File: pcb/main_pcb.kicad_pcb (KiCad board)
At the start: 2 copper layers, 62 x 67 mm, 43 parts, among them J1 Conn_01x06_Socket, J4 USB_C_Receptacle_USB2.0, Q1 Si2323DS, SW1 SW_Push, SW2 SW_Push, SW3 SW_Push, U1 ESP32-H2-MINI-1, U2 LM5165Y, Y1 32.768KHz

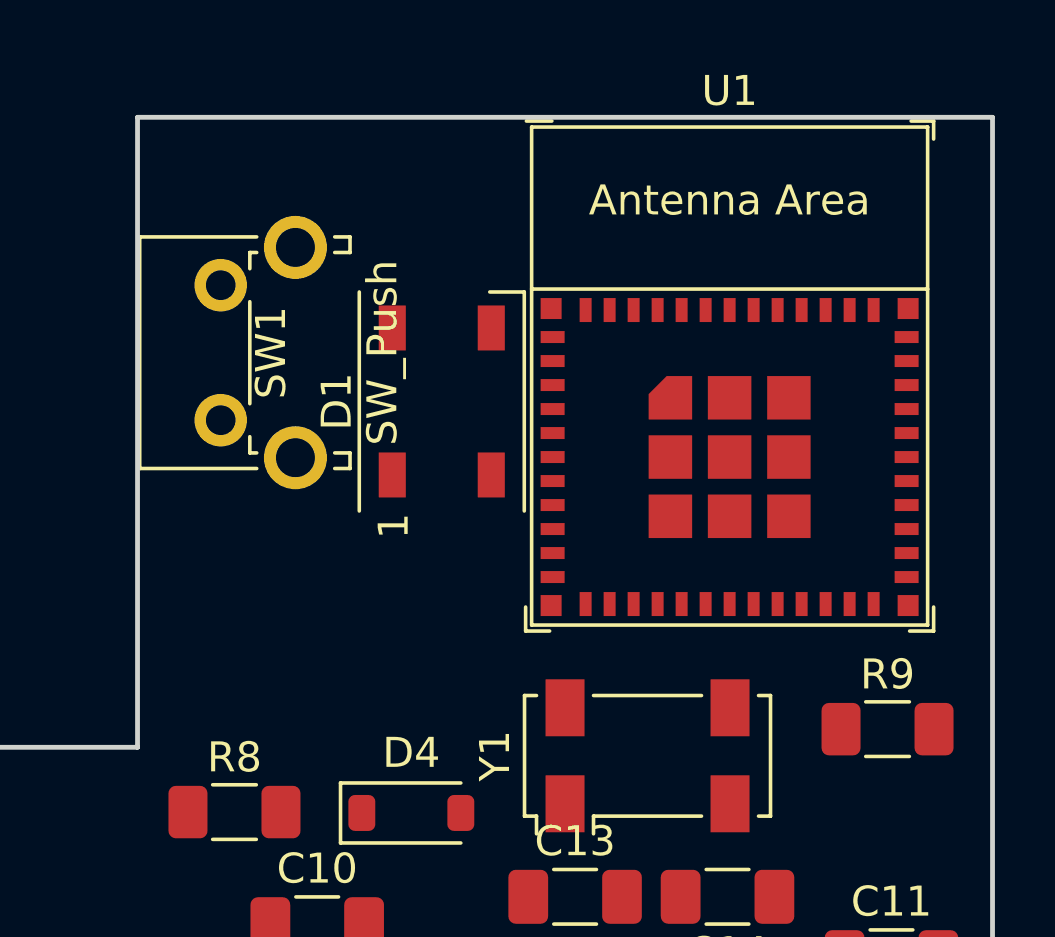
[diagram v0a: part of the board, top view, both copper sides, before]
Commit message: Change to 4 layer PCB
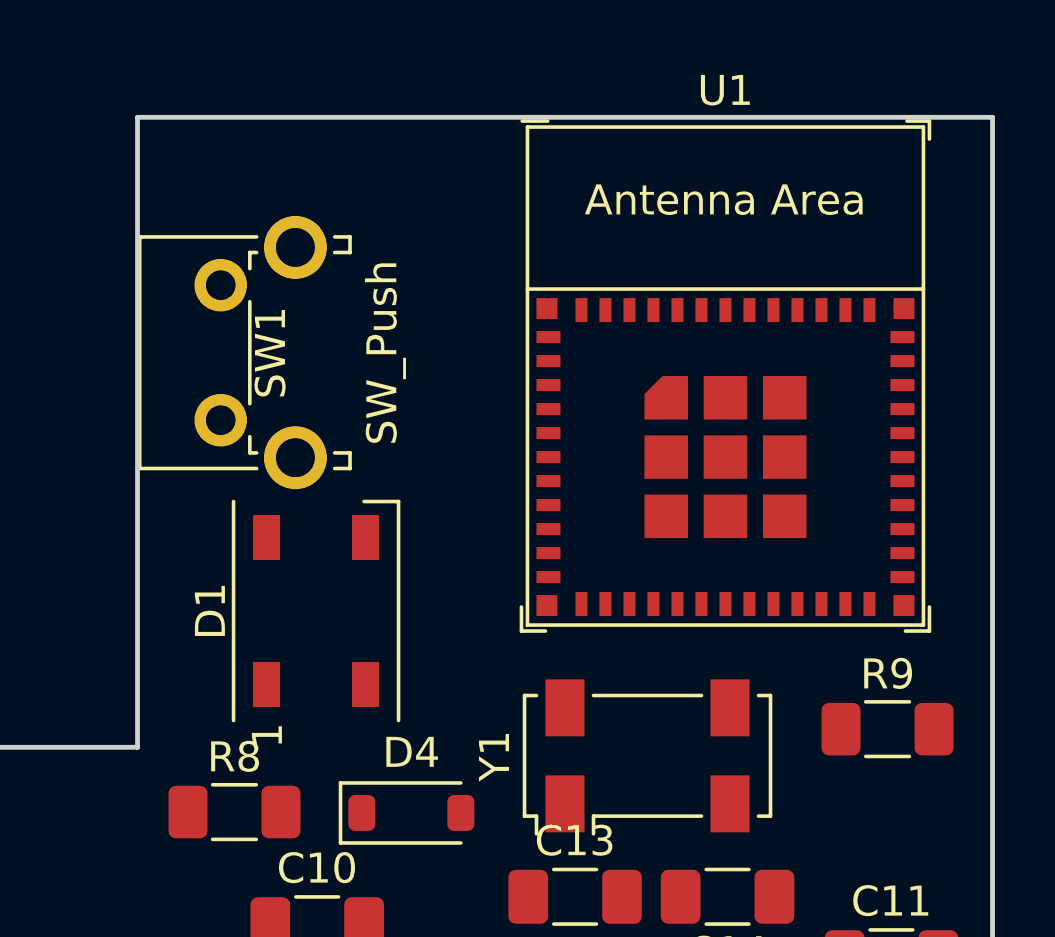
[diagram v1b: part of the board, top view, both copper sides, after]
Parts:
- moved D1 8.15 mm to (148.5, 59.7)
- moved U1 0.14 mm to (162.1, 51.9)
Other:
- copper layers 2 -> 4
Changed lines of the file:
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@@
   (layers
     (0 "F.Cu" signal)
+    (1 "In1.Cu" signal)
+    (2 "In2.Cu" signal)
     (31 "B.Cu" signal)
     (32 "B.Adhes" user "B.Adhesive")
@@
   )
   (setup
+    (stackup
+      (layer "F.SilkS" (type "Top Silk Screen"))
+      (layer "F.Paste" (type "Top Solder Paste"))
+      (layer "F.Mask" (type "Top Solder Mask") (thickness 0.01))
+      (layer "F.Cu" (type "copper") (thickness 0.035))
+      (layer "dielectric 1" (type "prepreg") (thickness 0.1) (material "FR4") (epsilon_r 4.5) (loss_tangent 0.02))
+      (layer "In1.Cu" (type "copper") (thickness 0.035))
+      (layer "dielectric 2" (type "core") (thickness 1.24) (material "FR4") (epsilon_r 4.5) (loss_tangent 0.02))
+      (layer "In2.Cu" (type "copper") (thickness 0.035))
+      (layer "dielectric 3" (type "prepreg") (thickness 0.1) (material "FR4") (epsilon_r 4.5) (loss_tangent 0.02))
+      (layer "B.Cu" (type "copper") (thickness 0.035))
+      (layer "B.Mask" (type "Bottom Solder Mask") (thickness 0.01))
+      (layer "B.Paste" (type "Bottom Solder Paste"))
+      (layer "B.SilkS" (type "Bottom Silk Screen"))
+      (copper_finish "None")
+      (dielectric_constraints no)
+    )
     (pad_to_mask_clearance 0)
     (pcbplotparams
@@
   )
   (footprint "PCM_Espressif:ESP32-H2-MINI-1" (layer "F.Cu")
-    (at 162.249 51.857)
+    (at 162.11 51.857)
     (descr "ESP32-H2-MINI-1: https://www.espressif.com/sites/default/files/documentation/esp32-h2-mini-1_mini-1u_datasheet_en.pdf")
     (tags "ESP32-H2")
@@
       (polygon
         (pts
-          (xy 168.849 48.957)
-          (xy 155.649 48.957)
-          (xy 155.649 43.557)
-          (xy 168.849 43.557)
+          (xy 168.71 48.957)
+          (xy 155.51 48.957)
+          (xy 155.51 43.557)
+          (xy 168.71 43.557)
         )
       )
@@
   )
   (footprint "LED_SMD:LED_WS2812B_PLCC4_5.0x5.0mm_P3.2mm" (layer "F.Cu")
-    (at 152.654 52.705 90)
+    (at 148.463 59.69 90)
     (descr "5.0mm x 5.0mm Addressable RGB LED NeoPixel, https://cdn-shop.adafruit.com/datasheets/WS2812B.pdf")
     (tags "LED RGB NeoPixel PLCC-4 5050")

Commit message: First rough PCB layout
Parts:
- removed C3: 1uF, Capacitor_SMD:C_1206_3216Metric_Pad1.33x1.80mm_HandSolder
- SW1: value SW_Push -> Pair
- SW2: value SW_Push -> Reset
- SW3: value SW_Push -> Boot
- moved C1 55.9 mm to (153.2, 48.9), turned to 90 degrees
- moved C2 54.0 mm to (153.2, 54.1), turned to -90 degrees
- moved R7 36.5 mm to (146.6, 44.7)
- moved R5 35.3 mm to (166.8, 64.0), turned to -90 degrees
- moved C4 31.1 mm to (167.5, 81.3), turned to 180 degrees
- moved R12 31.1 mm to (117.5, 65.8)
- moved C11 30.9 mm to (151.8, 44.7)
- moved R2 30.6 mm to (125.5, 81.9), turned to -90 degrees
- moved JP1 30.1 mm to (125.6, 86.5), turned to 90 degrees
- moved R4 28.9 mm to (127.9, 76.2), turned to -90 degrees
- moved R10 28.0 mm to (116.2, 69.6), turned to 90 degrees
- moved R11 26.8 mm to (118.5, 69.6), turned to 90 degrees
- moved R3 25.5 mm to (131.8, 76.2), turned to -90 degrees
- moved JP4 25.0 mm to (113.0, 66.2), turned to 0 degrees
- moved L1 23.2 mm to (134.2, 82.7), turned to -90 degrees
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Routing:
- net /EN: track 0.00 -> 57.5 mm
- net VBUS: track 0.00 -> 23.5 mm
- net Net-(C12-Pad1): track 0.00 -> 20.4 mm
- net /D+: track 0.00 -> 19.2 mm
- net /D-: track 0.00 -> 18.3 mm
- net VDD: track 0.00 -> 15.6 mm, vias 0 -> 1
- net /PAIR: track 0.00 -> 13.6 mm
- net Net-(D1-DIN): track 0.00 -> 11.4 mm
- net GND: track 0.00 -> 4.02 mm, vias 0 -> 1
- net Net-(J4-CC1): track 0.00 -> 2.80 mm
- net Net-(D3-A): track 0.00 -> 2.42 mm
- net Net-(J4-CC2): track 0.00 -> 2.41 mm
- added copper zone on In1.Cu, net GND
- added copper zone on In2.Cu, net VDD

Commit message: Improve PCB layout
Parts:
- added C15: 4.7uF, Capacitor_SMD:C_1206_3216Metric_Pad1.33x1.80mm_HandSolder, F.Cu at (128.5, 83.9)
- added C16: 4.7uF, Capacitor_SMD:C_1206_3216Metric_Pad1.33x1.80mm_HandSolder, F.Cu at (128.5, 81.5)
- added C3: 4.7uF, Capacitor_SMD:C_1206_3216Metric_Pad1.33x1.80mm_HandSolder, F.Cu at (128.5, 86.5)
- added R13: 59k, Resistor_SMD:R_1206_3216Metric_Pad1.30x1.75mm_HandSolder, F.Cu at (133.6, 102.4)
- added R14: 1.1, Resistor_SMD:R_1206_3216Metric_Pad1.30x1.75mm_HandSolder, F.Cu at (133.7, 83.2)
- C6: value 1uF -> 4.7uF
- C9: value 1uF -> 82nF
- L1: value 68uH -> 56uH; footprint Inductor_SMD:L_1206_3216Metric_Pad1.22x1.90mm_HandSolder -> Inductor_SMD:L_Wuerth_WE-PD2-Typ-L
- moved C9 24.5 mm to (128.5, 102.4)
- moved C7 18.0 mm to (128.5, 99.9), turned to 0 degrees
- moved R2 15.9 mm to (128.5, 97.5), turned to 0 degrees
- moved JP1 14.9 mm to (134.0, 98.8)
- moved C5 12.0 mm to (128.5, 91.3), turned to 0 degrees
- moved U2 11.9 mm to (131.1, 94.5), turned to 0 degrees
- moved C6 7.35 mm to (128.5, 88.9), turned to 180 degrees
- moved L1 5.95 mm to (135.4, 88.5), turned to 0 degrees
- moved C8 1.53 mm to (146.3, 75.9)
- moved R9 0.51 mm to (158.9, 67.9)
- moved R11 0.33 mm to (118.8, 69.6)
- moved R10 0.28 mm to (116.5, 69.6)
- moved JP4 0.09 mm to (113.0, 66.1)
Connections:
- C6 pad 1: +3.3V -> Net-(C15-Pad1)
- U2 pad 5: GND -> Net-(U2-RT)
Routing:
- net /TXD: track 0.00 -> 59.1 mm, vias 0 -> 2
- net /RXD: track 0.00 -> 56.6 mm, vias 0 -> 2
- net /DATA_IN: track 0.00 -> 47.1 mm, vias 0 -> 2
- net /D+: track 19.2 -> 61.2 mm
- net /D-: track 18.3 -> 59.0 mm
- net Net-(U1-GPIO9): track 0.00 -> 38.1 mm, vias 0 -> 2
- net /PAIR: track 13.6 -> 47.6 mm, vias 0 -> 1
- net /EN: track 57.5 -> 91.0 mm, vias 0 -> 2
- net GND: track 4.02 -> 25.8 mm, vias 1 -> 11
- net /LED: track 0.00 -> 15.9 mm, vias 0 -> 2
- net Net-(U1-GPIO14/XTAL_32K_N): track 0.00 -> 15.4 mm
- net Net-(U2-RT): track 0.00 -> 14.9 mm
- net Net-(U1-GPIO13/XTAL_32K_P): track 0.00 -> 14.2 mm
- net Net-(J1-Pin_2): track 0.00 -> 13.9 mm
- net Net-(U2-SW): track 0.00 -> 11.1 mm, vias 0 -> 2
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- added copper zone on F.Cu, net +3.3V
- added copper zone on In2.Cu, net +3.3V
- added copper zone on F.Cu, net GND
- added copper zone on F.Cu, net Net-(C15-Pad1)
- added copper zone on F.Cu, net VDD

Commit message: Update PCB layout
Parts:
- moved C11 19.2 mm to (169.7, 51.5), turned to 90 degrees
- moved C1 5.66 mm to (151.1, 54.2), turned to -90 degrees
- moved R7 1.22 mm to (145.3, 44.7)
- moved C2 0.31 mm to (153.5, 54.2)
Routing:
- net GND: track 25.8 -> 59.3 mm, vias 11 -> 30
- net +3.3V: track 2.34 -> 3.89 mm, vias 2 -> 5
- net /PAIR: track 47.6 -> 47.8 mm, vias 1 -> 2

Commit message: Fix DRC errors
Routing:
- net GND: track 59.3 -> 67.5 mm, vias 30 -> 33
- net VBUS: track 23.5 -> 24.4 mm
